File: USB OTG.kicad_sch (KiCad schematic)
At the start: 0 parts

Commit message: PMIC DCDC
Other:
- title: Leaf RV1126 Power -> Leaf RV1126 PMIC RK809
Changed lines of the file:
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@@
   (paper "A4")
   (title_block
-    (title "Leaf RV1126 Power")
+    (title "Leaf RV1126 PMIC RK809")
     (date "2023-02-23")
     (rev "1")

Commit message: updated: PMIC codec
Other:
- title: Leaf RV1126 PMIC RK809 -> Leaf RV1126 PMIC RK809 Codec
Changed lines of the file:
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@@
   (paper "A4")
   (title_block
-    (title "Leaf RV1126 PMIC RK809")
-    (date "2023-02-23")
+    (title "Leaf RV1126 PMIC RK809 Codec")
+    (date "2023-02-25")
     (rev "1")
     (company "Qingdao IotPi Information Technology")

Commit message: updated: titles
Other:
- title: Leaf RV1126 PMIC RK809 Codec -> Leaf RV1126 RK809 USB OTG
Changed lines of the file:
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@@
   (paper "A4")
   (title_block
-    (title "Leaf RV1126 PMIC RK809 Codec")
+    (title "Leaf RV1126 RK809 USB OTG")
     (date "2023-02-25")
     (rev "1")

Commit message: added USB
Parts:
- added J2: USB_OTG, symbol Connector:USB_OTG
- added U1: rv1126/rv1109, symbol CPU_Rockchip:rv1126_rv1109
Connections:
- new net VCC_0V8: U1.R6 (USB_AVDD_0V8)
- new net VCC_1V8: U1.R7 (USB_AVDD_1V8)
- new net VCC_3V3: U1.T7 (USB_AVDD_3V3)

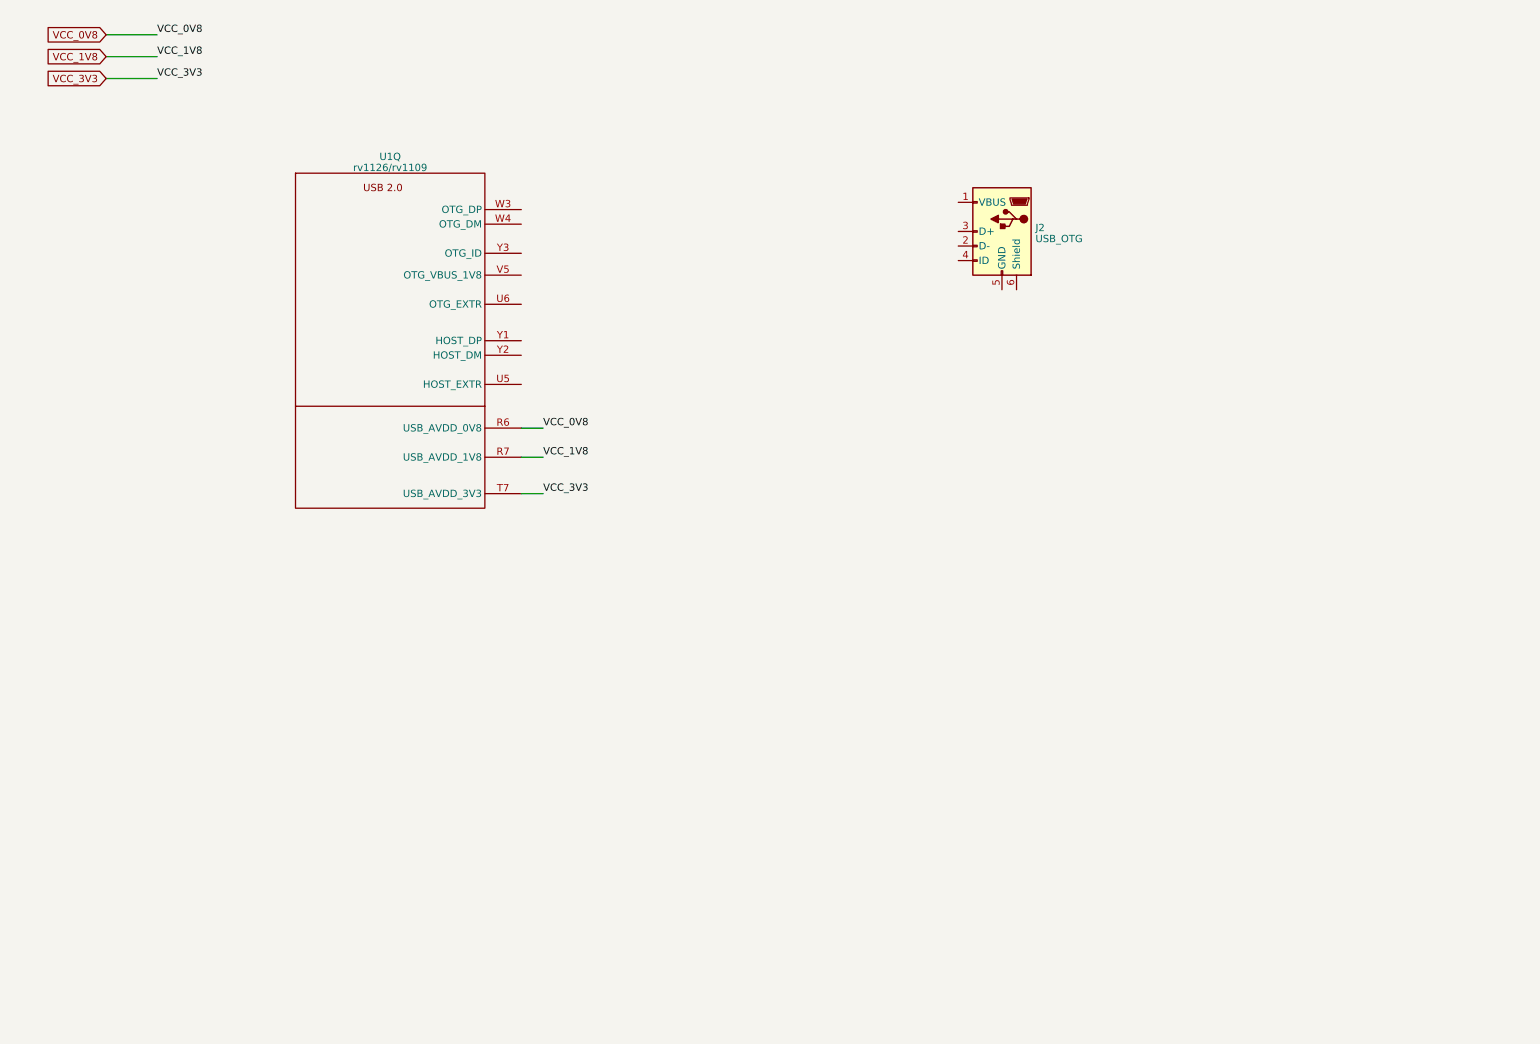
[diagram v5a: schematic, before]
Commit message: updated USB
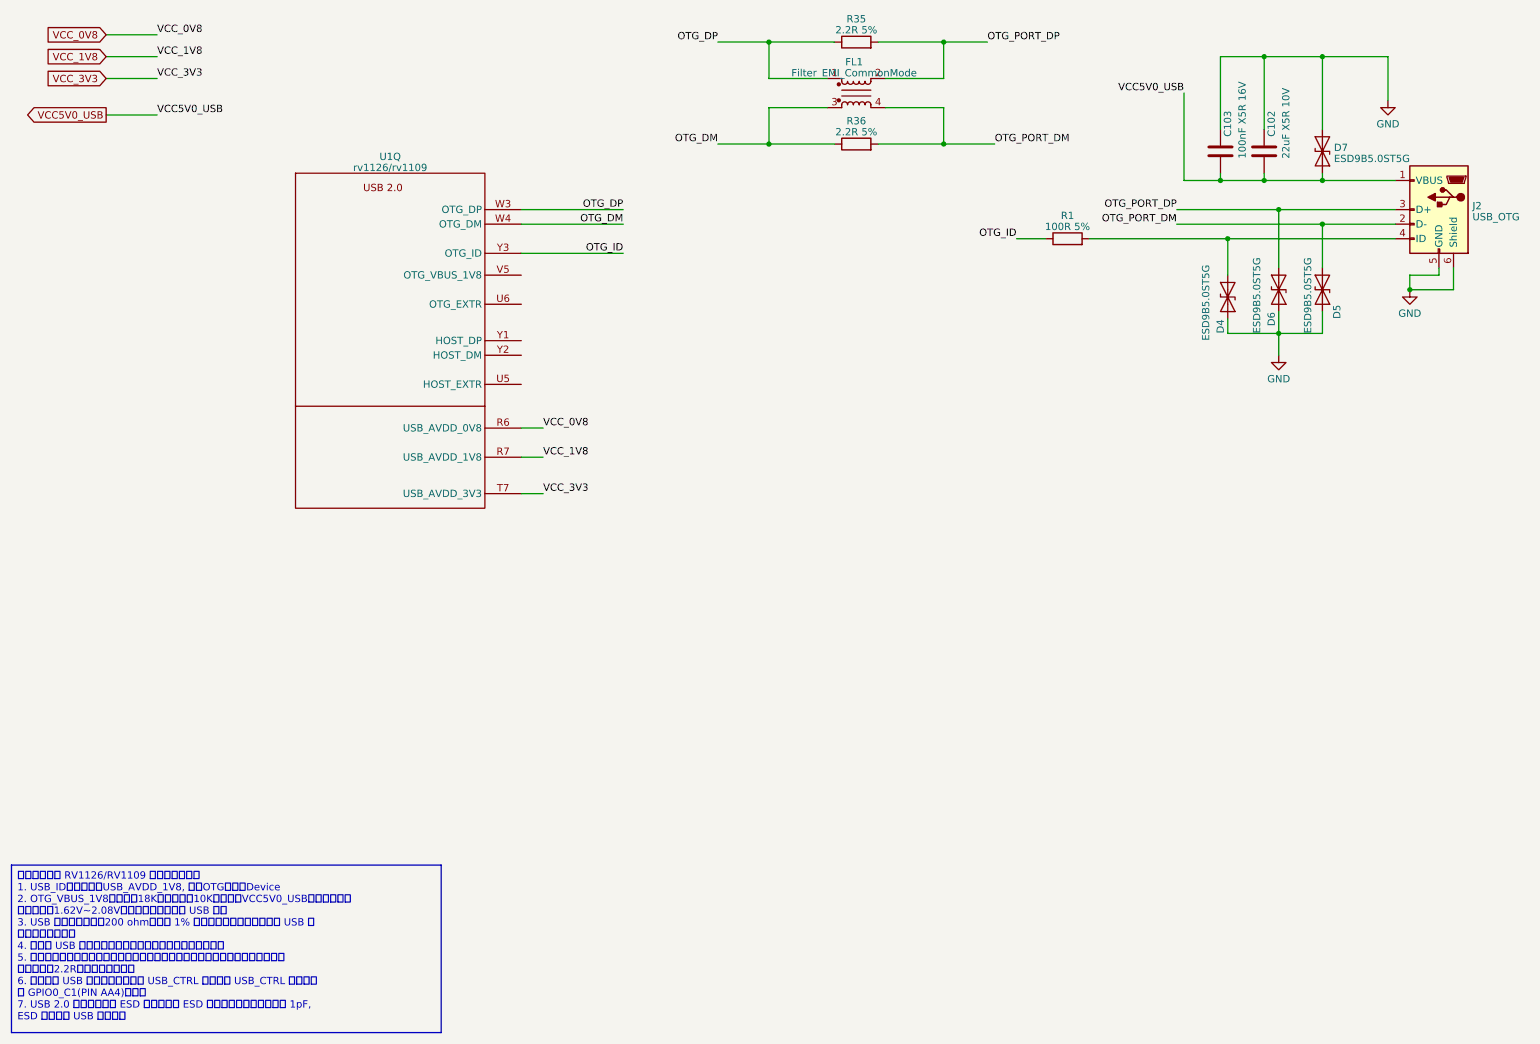
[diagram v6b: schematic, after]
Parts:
- added C102: 22uF X5R 10V, Capacitor_SMD:C_0805_2012Metric, symbol Device:C
- added C103: 100nF X5R 16V, Capacitor_SMD:C_0402_1005Metric, symbol Device:C
- added D4, D5, D6, D7: ESD9B5.0ST5G, Diode_SMD:D_SOD-923, symbol Diode:ESD9B5.0ST5G
- added FL1: Filter_EMI_CommonMode, Inductor_SMD:L_CommonModeChoke_Coilcraft_0603USB, symbol Device:Filter_EMI_CommonMode
- added R1: 100R 5%, Resistor_SMD:R_0402_1005Metric, symbol Device:R
- added R35, R36: 2.2R 5%, Resistor_SMD:R_0603_1608Metric, symbol Device:R
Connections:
- net VCC5V0_USB: now reaches J2.1 (VBUS)
- net VCC5V0_USB: now also C102.2, C103.2, D7.1 (A1)
- net OTG_PORT_DM: now reaches J2.2 (D-)
- net OTG_PORT_DM: now also D5.1 (A1), FL1.4, R36.2
- net OTG_PORT_DP: now reaches J2.3 (D+)
- net OTG_PORT_DP: now also D6.1 (A1), FL1.2, R35.2
- net at J2.4 (ID): now also D4.1 (A1), R1.2
- net GND: now reaches J2.5 (GND)
- net GND: now also J2.6 (Shield), C102.1, C103.1, D4.2 (A2), D5.2 (A2), D6.2 (A2), D7.2 (A2)
- net OTG_DP: now reaches U1.W3 (OTG_DP)
- net OTG_DP: now also FL1.1, R35.1
- net OTG_DM: now reaches U1.W4 (OTG_DM)
- net OTG_DM: now also FL1.3, R36.1
- net OTG_ID: now reaches U1.Y3 (OTG_ID)
- net OTG_ID: now also R1.1
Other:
- moved on the sheet: J2
